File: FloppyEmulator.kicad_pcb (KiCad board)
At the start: 2 copper layers, 5 parts, among them U1 STM32F405RGTx, X2 Conn_01x09, X3 Conn_02x17_Odd_Even, X4 Conn_01x04

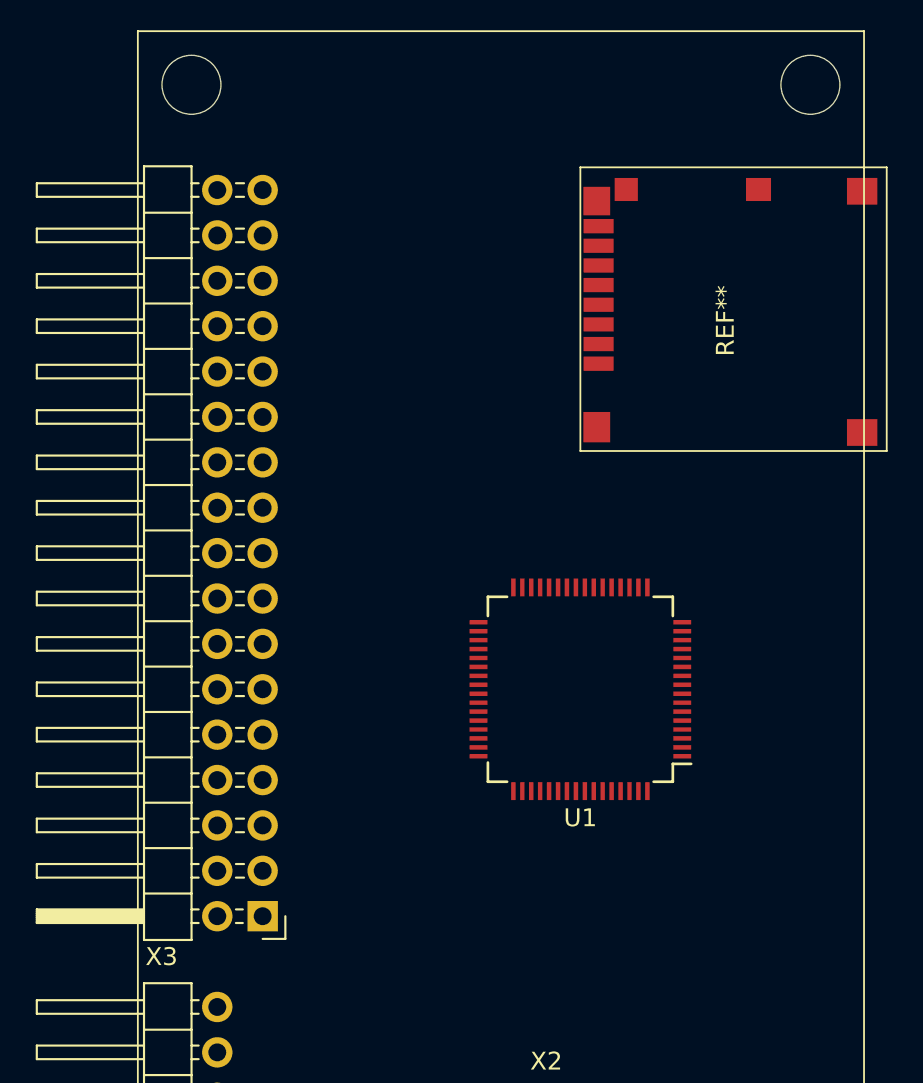
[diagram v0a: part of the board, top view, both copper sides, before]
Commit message: Add microSD footprint. Update schematic and PCB
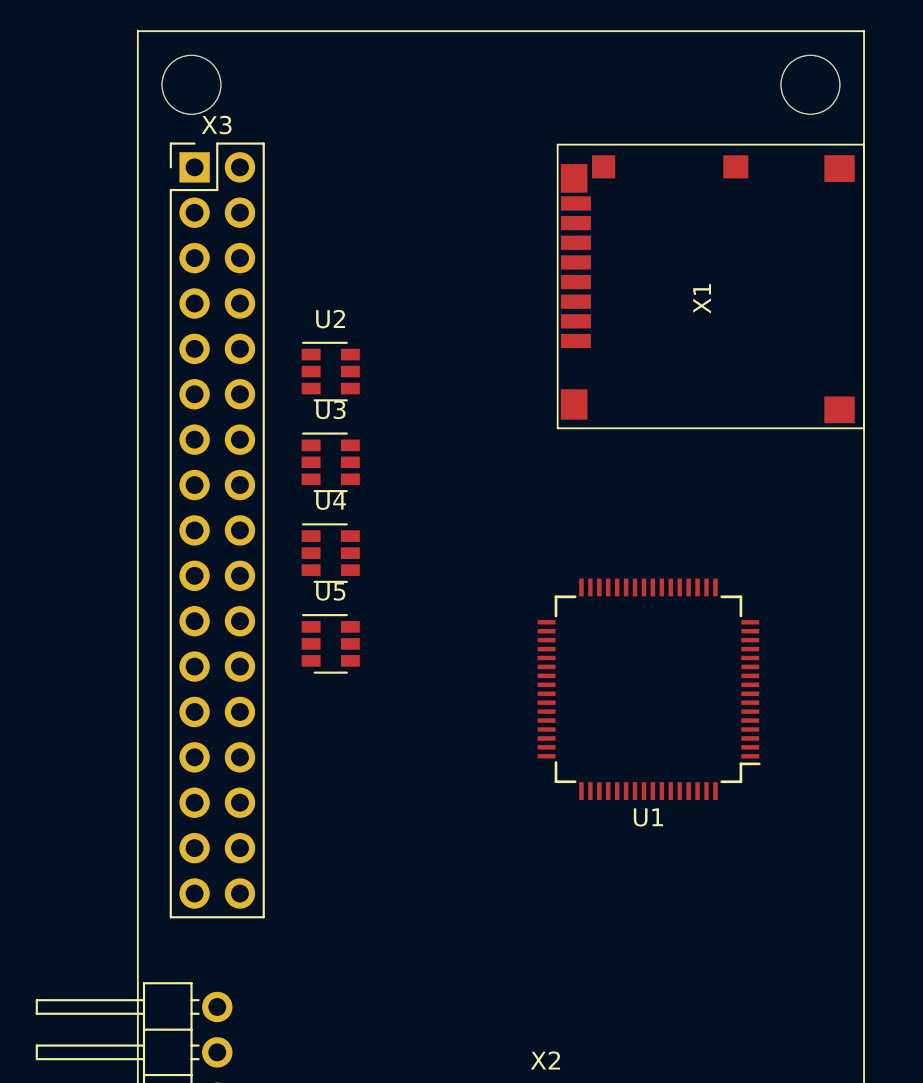
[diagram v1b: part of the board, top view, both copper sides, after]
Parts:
- removed REF**: MOLEX_5027740891, MOLEX_5027740891
- added U2: SN74LVC2G07, TO_SOT_Packages_SMD:SOT-23-6, F.Cu at (161.3, 40.6)
- added U3: SN74LVC2G07, TO_SOT_Packages_SMD:SOT-23-6, F.Cu at (161.3, 45.7)
- added U4: SN74LVC2G07, TO_SOT_Packages_SMD:SOT-23-6, F.Cu at (161.3, 50.8)
- added U5: SN74LVC2G07, TO_SOT_Packages_SMD:SOT-23-6, F.Cu at (161.3, 55.9)
- added X1: Micro_SD_Card_Det, components:MOLEX_5027740891, F.Cu at (181.6, 49.5)
- X3: footprint Pin_Headers:Pin_Header_Angled_2x17_Pitch2.54mm -> Pin_Headers:Pin_Header_Straight_2x17_Pitch2.54mm
- moved X3 42.1 mm to (153.7, 29.2), turned to 0 degrees
- moved U1 3.81 mm to (179.1, 58.4)
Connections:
- U1 pad 24: Net-(U1-Pad24) -> /CARD_DETECT

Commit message: Add ALPS 5-way joystick
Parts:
- added SW1: ALPS_5WAY, components:ALPS_SKRHABE010, F.Cu at (197.6, 70.0)
- added U6: SN74LVC2G07, TO_SOT_Packages_SMD:SOT-23-6, F.Cu at (161.3, 61.0)
- added U7: SN74LVC2G07, TO_SOT_Packages_SMD:SOT-23-6, F.Cu at (161.3, 67.3)

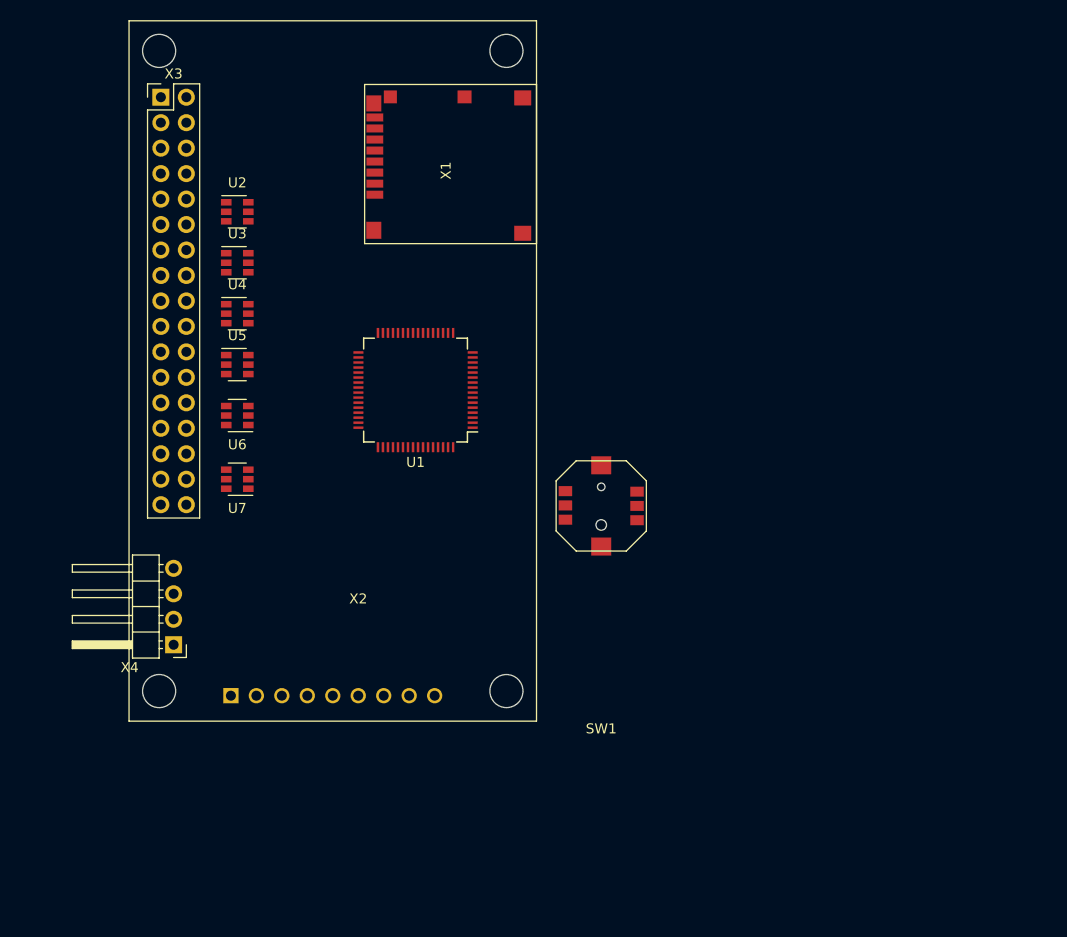
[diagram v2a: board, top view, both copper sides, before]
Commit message: Add CubeMX layout pic. PCB remastered
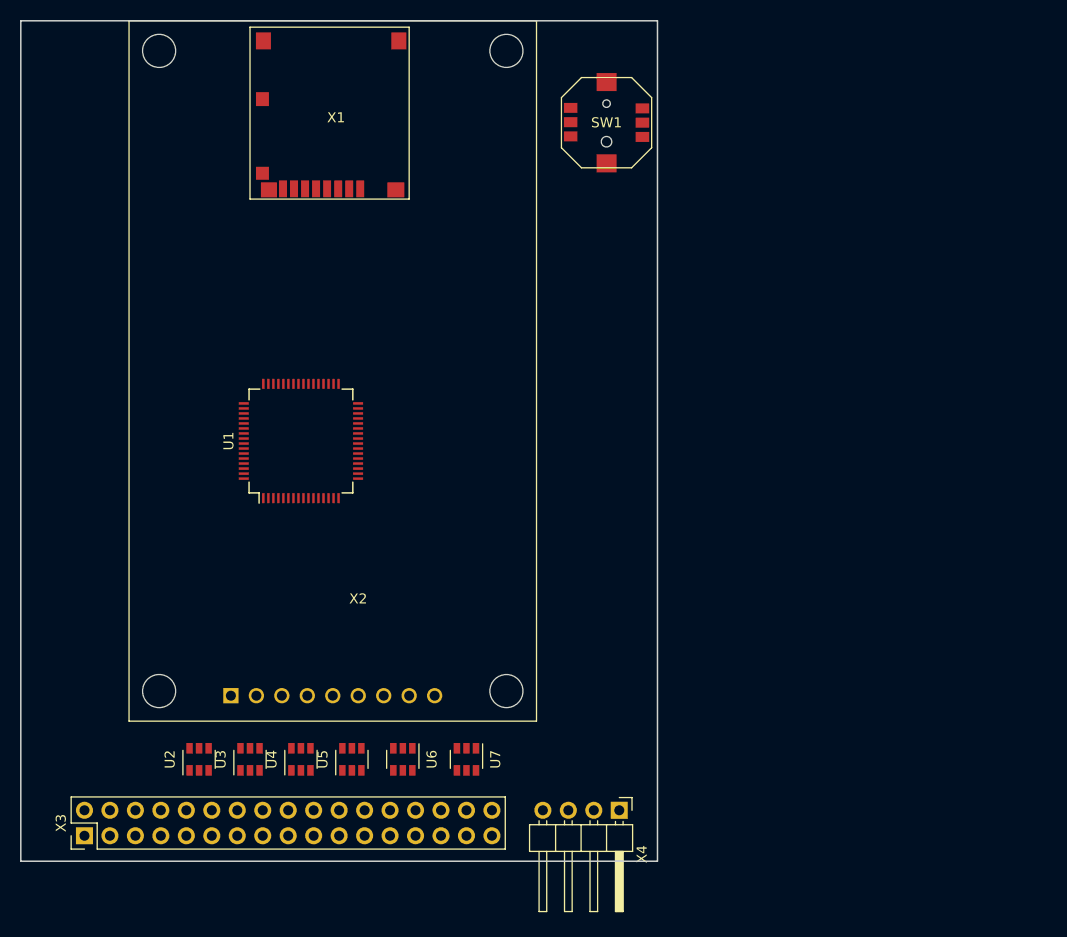
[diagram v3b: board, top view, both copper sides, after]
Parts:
- moved X3 74.1 mm to (146.1, 102.9), turned to 90 degrees
- moved U2 54.7 mm to (157.5, 95.2), turned to 90 degrees
- moved U3 49.5 mm to (162.6, 95.2), turned to 90 degrees
- moved X4 47.4 mm to (199.4, 100.3), turned to 270 degrees
- moved U4 44.9 mm to (167.6, 95.2), turned to 90 degrees
- moved U5 41.0 mm to (172.7, 95.2), turned to 90 degrees
- moved SW1 38.2 mm to (198.1, 31.8)
- moved U6 38.1 mm to (177.8, 95.2), turned to 270 degrees
- moved U7 36.1 mm to (184.2, 95.2), turned to 270 degrees
- moved X1 18.0 mm to (184.2, 31.8), turned to 180 degrees
- moved U1 12.5 mm to (167.6, 63.5), turned to 90 degrees
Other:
- board outline added: 63.5 x 83.8 mm

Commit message: Up
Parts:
- added U8: SN74LVC2G07, TO_SOT_Packages_SMD:SOT-23-6, F.Cu at (147.3, 95.2)
- added U9: SN74LVC2G07, TO_SOT_Packages_SMD:SOT-23-6, F.Cu at (152.4, 95.2)
- moved X1 60.0 mm to (190.5, 91.4), turned to 90 degrees
- moved X2 32.6 mm to (143.5, 71.1), turned to 270 degrees
- moved U1 14.6 mm to (167.0, 78.1)
- moved U7 1.27 mm to (182.9, 95.2)
- turned SW1 to 45 degrees
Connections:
- net Net-(Q1-Pad1) renamed /OSC_OUT
- net Net-(Q1-Pad3) renamed /OSC_IN
- net Net-(U7-Pad1) renamed /RDY
- U1 pad 10: /WRGATE -> /STEP
- U1 pad 11: /WRDATA -> /DIR
- U1 pad 14: /SEL0 -> /WRDATA
- U1 pad 15: /SEL1 -> /WRGATE
- U1 pad 16: /SEL2 -> /TRACK0
- U1 pad 17: /SEL3 -> /WPROT
- U1 pad 3: /TRACK0 -> /SEL0
- U1 pad 4: /WPROT -> /SEL1
- U1 pad 8: /SIDE -> /SEL2
- U1 pad 9: /STEP -> /SEL3
- U3 pad 5: Net-(U3-Pad5) -> Net-(U2-Pad5)
- U4 pad 5: Net-(U4-Pad5) -> Net-(U2-Pad5)
- U5 pad 5: Net-(U5-Pad5) -> Net-(U2-Pad5)
- U6 pad 1: Net-(U6-Pad1) -> /WPROT
- U6 pad 3: Net-(U6-Pad3) -> /TRACK0
- U7 pad 3: Net-(U7-Pad3) -> SPI2_MOSI
- U7 pad 5: Net-(U7-Pad5) -> Net-(U6-Pad5)

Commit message: Layout and schematic update
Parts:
- added C1: 0,1, Capacitors_SMD:C_0603, F.Cu at (232.3, 46.7)
- added C2: 0,1, Capacitors_SMD:C_0603, F.Cu at (232.3, 51.4)
- added C3: 0,1, Capacitors_SMD:C_0603, F.Cu at (235.1, 46.7)
- added C4: 0,1, Capacitors_SMD:C_0603, F.Cu at (238.0, 46.7)
- added C5: 0,1, Capacitors_SMD:C_0603, F.Cu at (240.8, 46.7)
- added Q2: BC817, TO_SOT_Packages_SMD:SOT-23, F.Cu at (171.4, 67.3)
- added R1: 10K, Resistors_SMD:R_0603, F.Cu at (167.6, 68.6)
- added X5: SWD, Pin_Headers:Pin_Header_Angled_1x04_Pitch2.54mm, F.Cu at (151.1, 67.3)
- SW1: moved to B.Cu
- X4: value Conn_01x04 -> TE 171826-4; footprint Pin_Headers:Pin_Header_Angled_1x04_Pitch2.54mm -> components:171826-4
- moved SW1 53.6 mm to (203.2, 85.1), turned to 315 degrees
- moved X1 22.7 mm to (200.7, 71.1)
- moved X4 8.03 mm to (196.8, 92.7), turned to 180 degrees
- moved X2 6.48 mm to (142.2, 77.5)
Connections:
- net Net-(U1-Pad1) renamed /VBAT
- net Net-(U1-Pad30) renamed /LED1
- net Net-(U1-Pad31) renamed /VCAP1
- net Net-(U1-Pad47) renamed /VCAP2
- net Net-(U1-Pad60) renamed /BOOT0
- net Net-(U1-Pad7) renamed /NRST
- SW1 pad 1: Net-(SW1-Pad1) -> /BUTTON2
- SW1 pad 2: Net-(SW1-Pad2) -> /BUTTON5
- SW1 pad 3: Net-(SW1-Pad3) -> /BUTTON3
- SW1 pad 4: Net-(SW1-Pad4) -> /BUTTON4
- SW1 pad 5: Net-(SW1-Pad5) -> GND
- SW1 pad 6: Net-(SW1-Pad6) -> /BUTTON1
- U1 pad 25: Net-(U1-Pad25) -> /BUTTON1
- U1 pad 26: Net-(U1-Pad26) -> /BUTTON2
- U1 pad 27: Net-(U1-Pad27) -> /BUTTON3
- U1 pad 28: Net-(U1-Pad28) -> /BUTTON4
- U1 pad 29: Net-(U1-Pad29) -> /BUTTON5
- U1 pad 41: BEEP -> /BEEP
- U1 pad 46: SWDIO -> /SWDIO
- U1 pad 49: SWCLK -> /SWCLK
- U1 pad 56: /BUTTON1 -> Net-(U1-Pad56)
- U1 pad 57: /BUTTON2 -> Net-(U1-Pad57)
- U1 pad 58: /BUTTON3 -> Net-(U1-Pad58)
- U1 pad 59: /BUTTON4 -> Net-(U1-Pad59)
- U2 pad 5: Net-(U2-Pad5) -> +3V3
- U3 pad 5: Net-(U2-Pad5) -> +3V3
- U4 pad 5: Net-(U2-Pad5) -> +3V3
- U5 pad 5: Net-(U2-Pad5) -> +3V3
- U6 pad 5: Net-(U6-Pad5) -> +5VDC
- U7 pad 5: Net-(U6-Pad5) -> +5VDC
- U9 pad 5: Net-(U6-Pad5) -> +5VDC
- X1 pad 4: Net-(X1-Pad4) -> +3V3
- X3 pad 1: Net-(X3-Pad1) -> GND
- X3 pad 11: Net-(X3-Pad11) -> GND
- X3 pad 13: Net-(X3-Pad13) -> GND
- X3 pad 15: Net-(X3-Pad15) -> GND
- X3 pad 17: Net-(X3-Pad17) -> GND
- X3 pad 19: Net-(X3-Pad19) -> GND
- X3 pad 21: Net-(X3-Pad21) -> GND
- X3 pad 23: Net-(X3-Pad23) -> GND
- X3 pad 25: Net-(X3-Pad25) -> GND
- X3 pad 27: Net-(X3-Pad27) -> GND
- X3 pad 29: Net-(X3-Pad29) -> GND
- X3 pad 31: Net-(X3-Pad31) -> GND
- X3 pad 33: Net-(X3-Pad33) -> GND
- X3 pad 5: Net-(X3-Pad5) -> GND
- X3 pad 7: Net-(X3-Pad7) -> GND
- X3 pad 9: Net-(X3-Pad9) -> GND
- X4 pad 1: Net-(X4-Pad1) -> +5VDC
- X4 pad 2: Net-(X4-Pad2) -> GND
- X4 pad 3: Net-(X4-Pad3) -> GND
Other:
- board size 63.5 x 83.8 mm -> 69.9 x 48.3 mm

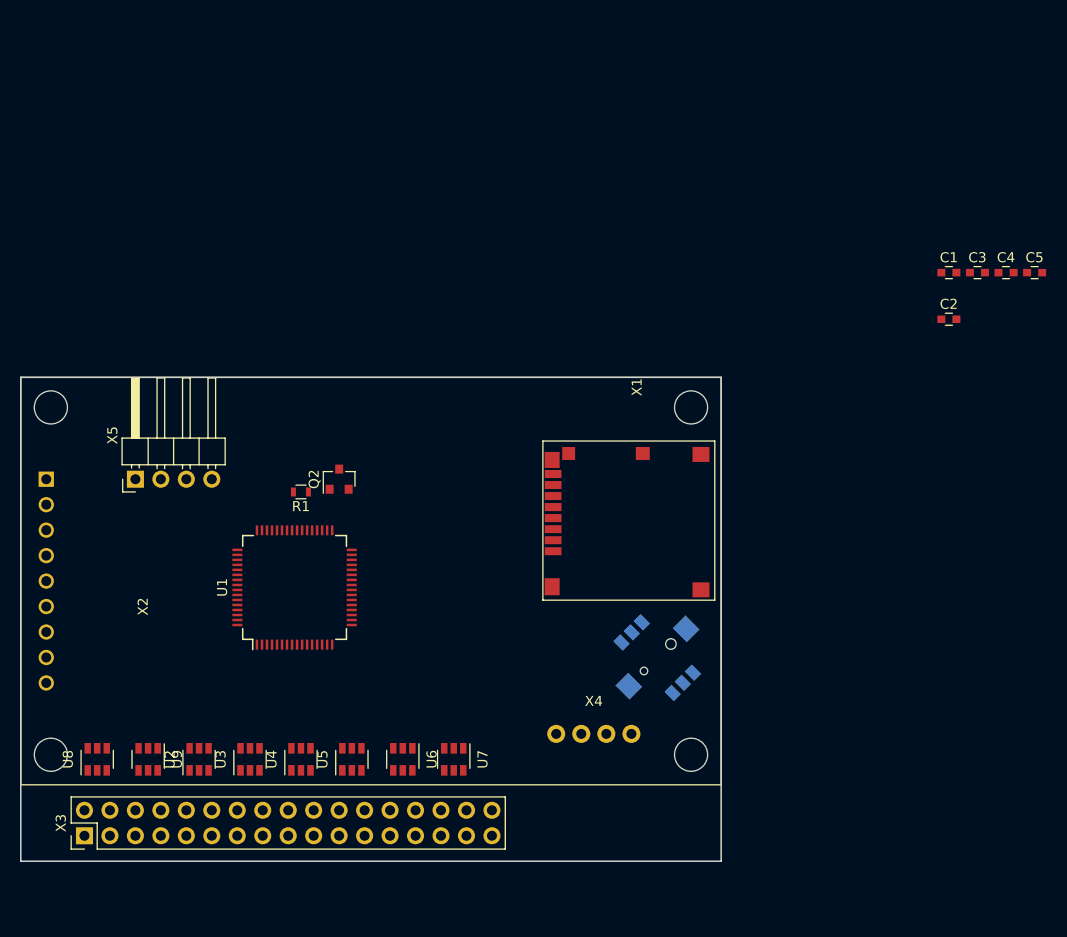
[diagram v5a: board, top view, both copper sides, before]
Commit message: Caps added. PCB update
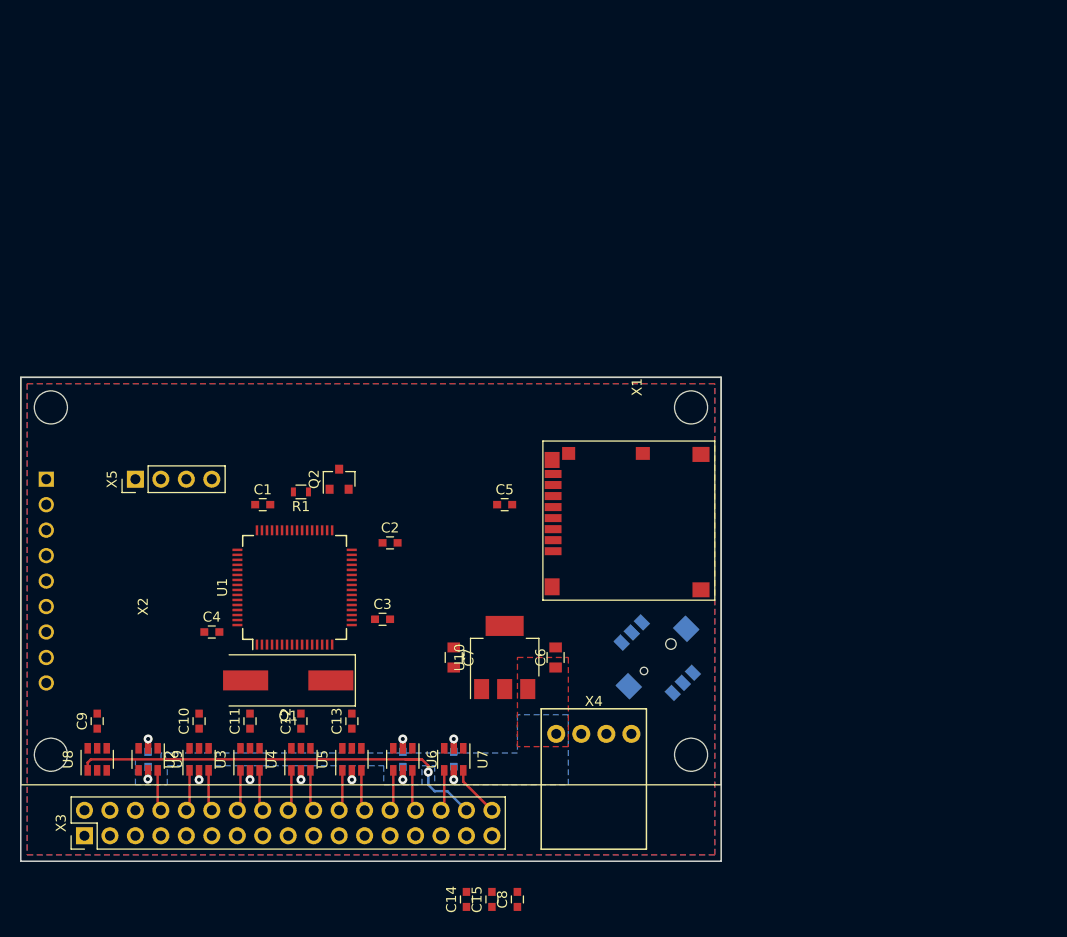
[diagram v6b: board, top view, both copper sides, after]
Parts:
- added C10: 0,1, Capacitors_SMD:C_0603, F.Cu at (157.5, 91.4)
- added C11: 0,1, Capacitors_SMD:C_0603, F.Cu at (162.6, 91.4)
- added C12: 0,1, Capacitors_SMD:C_0603, F.Cu at (167.6, 91.4)
- added C13: 0,1, Capacitors_SMD:C_0603, F.Cu at (172.7, 91.4)
- added C14: 0,1, Capacitors_SMD:C_0603, F.Cu at (184.2, 109.2)
- added C15: 0,1, Capacitors_SMD:C_0603, F.Cu at (186.7, 109.2)
- added C16: 0,1, Capacitors_SMD:C_0603, B.Cu at (152.4, 95.2)
- added C17: 0,1, Capacitors_SMD:C_0603, B.Cu at (182.9, 95.2)
- added C18: 0,1, Capacitors_SMD:C_0603, B.Cu at (177.8, 95.2)
- added C6: 2u2, Capacitors_SMD:C_0805, F.Cu at (193.0, 85.1)
- added C7: 2u2, Capacitors_SMD:C_0805, F.Cu at (182.9, 85.1)
- added C8: 0,1, Capacitors_SMD:C_0603, F.Cu at (189.2, 109.2)
- added C9: 0,1, Capacitors_SMD:C_0603, F.Cu at (147.3, 91.4)
- added Q1: Crystal_GND24, Crystals:Crystal_SMD_HC49-SD, F.Cu at (166.4, 87.4)
- added U10: AP1117-15, TO_SOT_Packages_SMD:SOT-223-3_TabPin2, F.Cu at (188.0, 85.1)
- X4: footprint components:171826-4 -> 171826-4
- X5: footprint Pin_Headers:Pin_Header_Angled_1x04_Pitch2.54mm -> Pin_Headers:Pin_Header_Straight_1x04_Pitch2.54mm
- moved C4 86.9 mm to (158.8, 82.5)
- moved C1 72.2 mm to (163.8, 69.8)
- moved C3 68.7 mm to (175.8, 81.3)
- moved C2 60.0 mm to (176.5, 73.7)
- moved C5 57.7 mm to (188.0, 69.8)
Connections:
- U1 pad 59: Net-(U1-Pad59) -> /SIDE
- U8 pad 2: Net-(U8-Pad2) -> GND
- U8 pad 5: Net-(U8-Pad5) -> +3V3
- U9 pad 2: Net-(U9-Pad2) -> GND
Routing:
- net Net-(U8-Pad1): track 0.00 -> 43.6 mm, vias 0 -> 1
- net GND: track 0.00 -> 10.3 mm, vias 0 -> 7
- net +5VDC: track 0.00 -> 5.66 mm, vias 0 -> 3
- net Net-(U7-Pad6): track 0.00 -> 5.16 mm
- net Net-(U5-Pad3): track 0.00 -> 4.11 mm
- net Net-(U5-Pad1): track 0.00 -> 4.11 mm
- net Net-(U3-Pad3): track 0.00 -> 4.11 mm
- net Net-(U3-Pad1): track 0.00 -> 4.11 mm
- net Net-(U9-Pad6): track 0.00 -> 4.11 mm
- net Net-(U7-Pad4): track 0.00 -> 4.11 mm
- net Net-(U6-Pad6): track 0.00 -> 4.11 mm
- net Net-(U6-Pad4): track 0.00 -> 4.11 mm
- net Net-(U4-Pad3): track 0.00 -> 4.11 mm
- net Net-(U4-Pad1): track 0.00 -> 4.11 mm
- net Net-(U2-Pad3): track 0.00 -> 4.11 mm
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- added copper zone on B.Cu, net +5VDC
- added copper zone on F.Cu, net +5VDC
- added copper zone on B.Cu, net GND
- added copper zone on F.Cu, net GND
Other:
- net class Default: clearance 0 -> 0.2; via_dia 0.8 -> 0.9
- net class Power added: clearance 0.2, trace_width 0.5, via_dia 0.9, via_drill 0.4
- rule trace_clearance: 0 -> 0.2
- rule via_min_drill: 0.3 -> 0.4
- rule via_min_size: 0.4 -> 0.9

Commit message: Routing WIP
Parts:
- added C19: 15pF, Capacitors_SMD:C_0603, B.Cu at (158.8, 85.7)
- added C20: 15pF, Capacitors_SMD:C_0603, B.Cu at (168.9, 85.7)
- Q1: footprint Crystals:Crystal_SMD_HC49-SD -> Crystals:Crystal_HC49-U_Vertical
- moved C8 60.2 mm to (144.8, 68.6), turned to 270 degrees
- moved X5 8.13 mm to (156.2, 61.0)
- moved C5 2.30 mm to (190.2, 70.1), turned to 90 degrees
- moved C2 2.16 mm to (175.0, 72.1)
- moved C1 2.01 mm to (161.9, 69.2), turned to 180 degrees
- moved Q1 1.65 mm to (166.4, 85.7)
- moved U1 1.27 mm to (167.0, 76.8)
- moved C4 1.27 mm to (158.8, 81.3), turned to 180 degrees
- moved C3 0.82 mm to (175.3, 80.6)
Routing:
- net SPI1_MOSI: track 0.00 -> 41.4 mm
- net /CARD_DETECT: track 0.00 -> 38.8 mm
- net /SIDE: track 0.00 -> 26.1 mm
- net SPI1_MISO: track 0.00 -> 24.8 mm
- net SPI1_SCK: track 0.00 -> 23.6 mm
- net SPI1_NSS: track 0.00 -> 22.4 mm
- net /INDEX: track 0.00 -> 20.0 mm
- net /SEL0: track 0.00 -> 17.0 mm
- net /SEL1: track 0.00 -> 16.4 mm
- net /SEL2: track 0.00 -> 16.3 mm
- net /WPROT: track 0.00 -> 16.1 mm
- net /SEL3: track 0.00 -> 15.2 mm
- net /TRACK0: track 0.00 -> 14.2 mm
- net /SWCLK: track 0.00 -> 13.6 mm
- net /WRGATE: track 0.00 -> 13.0 mm
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- added copper zone on F.Cu, net +3V3
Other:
- net class Default: trace_width 0.25 -> 0.2
